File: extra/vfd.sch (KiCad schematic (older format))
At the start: 20 parts

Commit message: more updates, mostly notes and input/output direction changes
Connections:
- net 5v is gone; now on net VCC: P?.2 (P2)
- net GND: now also U?.19 (CE)
- net VCC: now also U?.1 (A->B)
- net vfdD7: now also U?.9 (A7)
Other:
- note added: "NOTE should protect digital ins and outs.. resistors on outs.. diodes on both ins and outs?"
- note added: "NOTE\n\nTo ensure the high-impedance state during power up or power down, OE should be tied to VCC through a pull-up resistor;\nthe minimum value of the resistor is determined by the current-sinking capability of the driver.\n\nboth input and output chips indicate this"

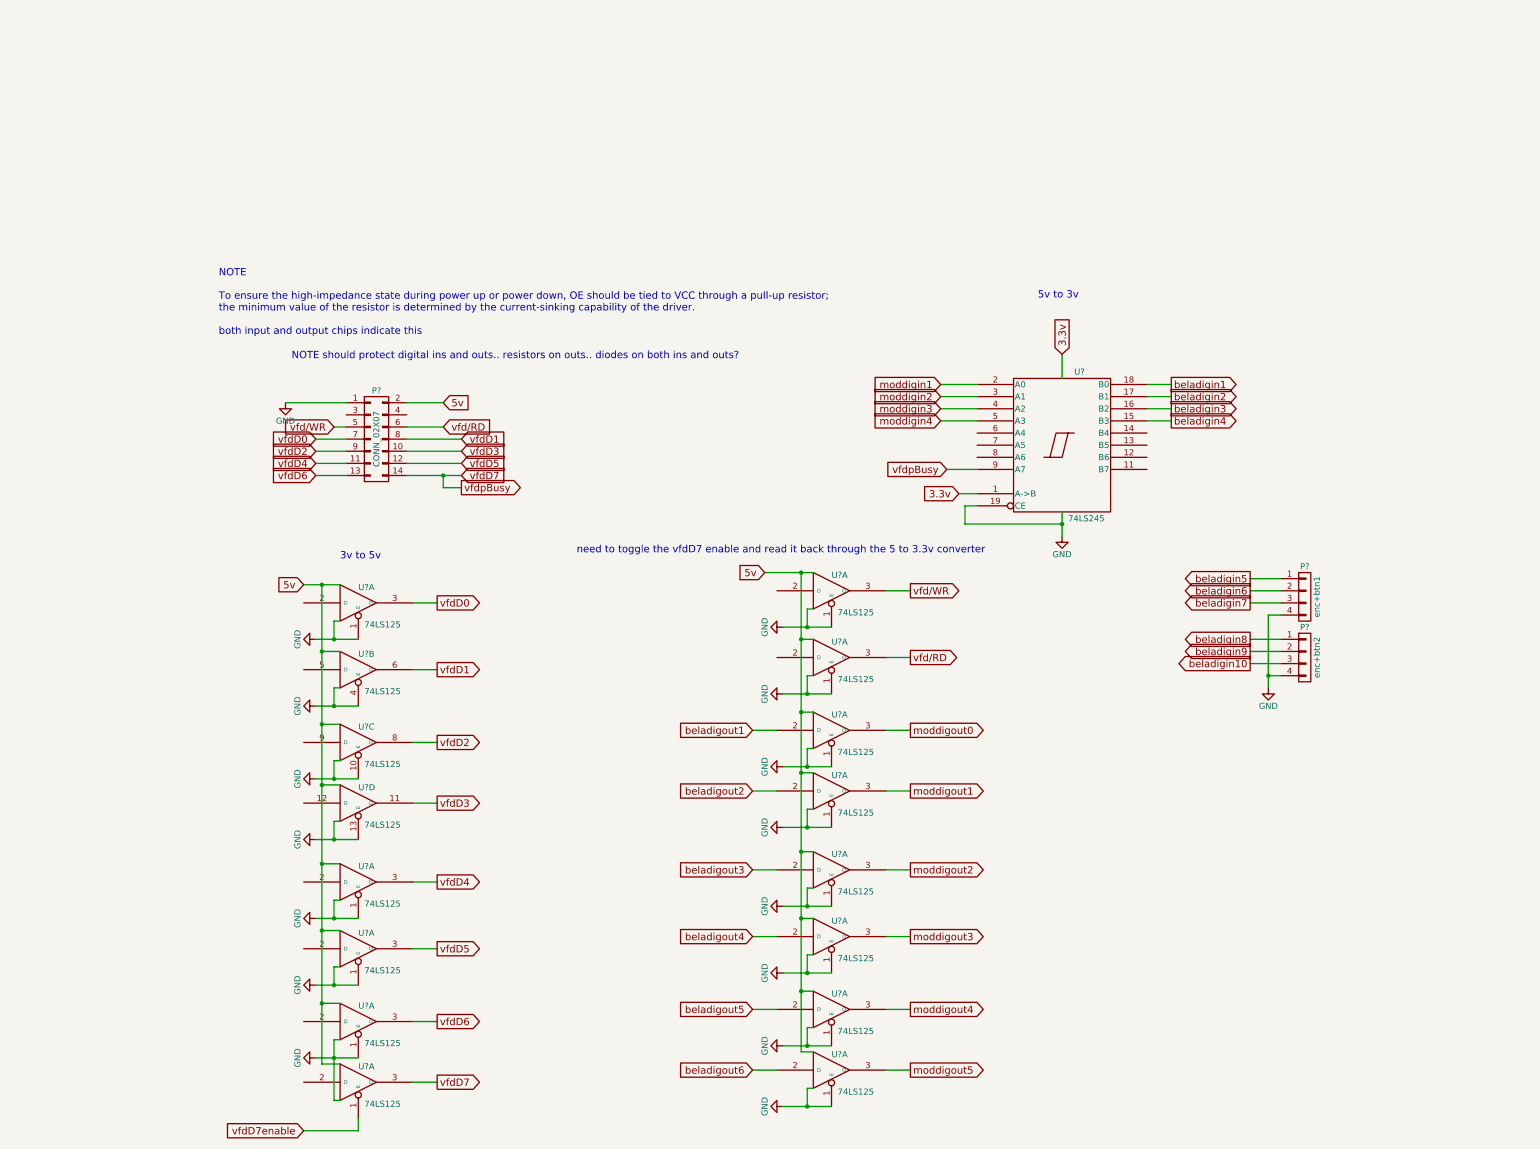
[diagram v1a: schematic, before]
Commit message: much more work on vfd [2 parallel interfaces]
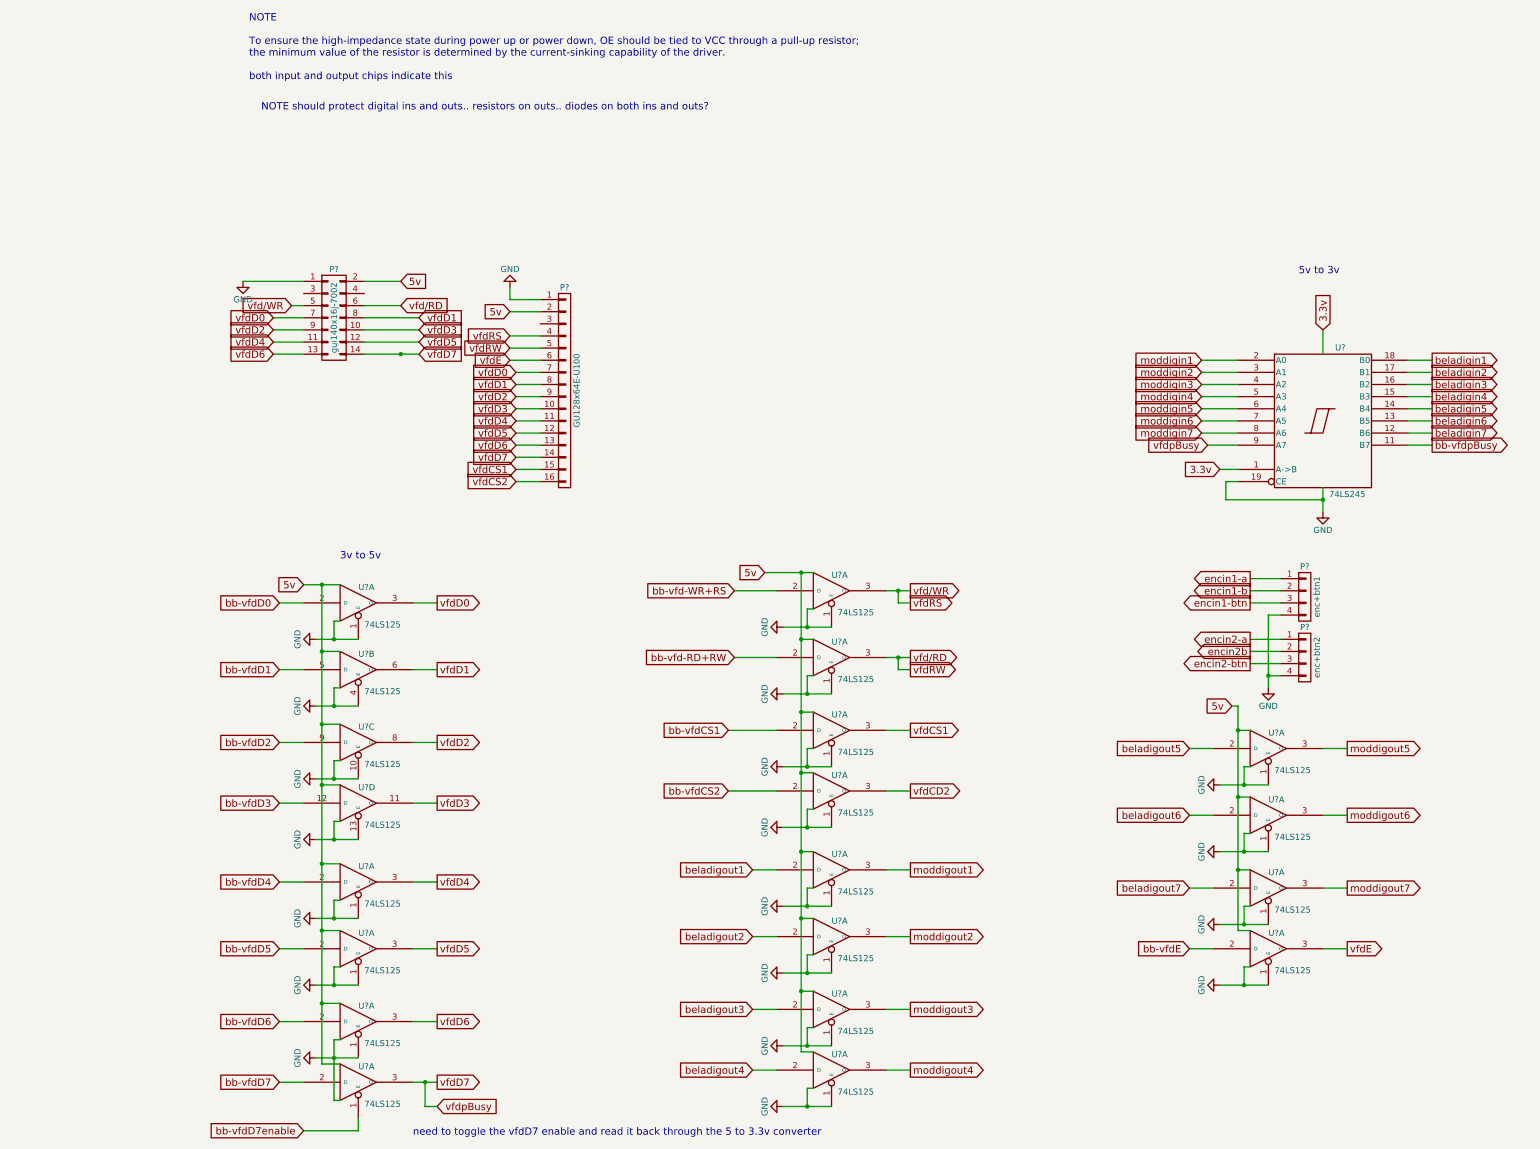
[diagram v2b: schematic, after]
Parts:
- added P?: GU128x64E-U100, symbol CONN_01X16
- added U? (x4): 74LS125, symbol 74LS125
- P?: value CONN_02X07 -> gui140x16j-7002
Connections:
- net GND: now also P?.1 (P1), U?.1 (E), U?.1 (E), U?.1 (E), U?.1 (E), U?.7 (GND), U?.7 (GND), U?.7 (GND), U?.7 (GND)
- net VCC: now also P?.2 (P2), U?.14 (VCC), U?.14 (VCC), U?.14 (VCC), U?.14 (VCC)
- net beladigin5: now also U?.14 (B4); no longer P?.1 (P1)
- net beladigin6: now also U?.13 (B5); no longer P?.2 (P2)
- net beladigin7: now also U?.12 (B6); no longer P?.3 (P3)
- net beladigout1: now also U?.2 (D); no longer U?.2 (D)
- net beladigout2: now also U?.2 (D); no longer U?.2 (D)
- net beladigout3: now also U?.2 (D); no longer U?.2 (D)
- net beladigout4: now also U?.2 (D); no longer U?.2 (D)
- net beladigout5: now also U?.2 (D); no longer U?.2 (D)
- net beladigout6: now also U?.2 (D); no longer U?.2 (D)
- net moddigout1: now also U?.3 (O); no longer U?.3 (O)
- net moddigout2: now also U?.3 (O); no longer U?.3 (O)
- net moddigout3: now also U?.3 (O); no longer U?.3 (O)
- net moddigout4: now also U?.3 (O); no longer U?.3 (O)
- net moddigout5: now also U?.3 (O); no longer U?.3 (O)
- net vfd/RD: now also P?.5 (P5)
- net vfd/WR: now also P?.4 (P4)
- net vfdD0: now also P?.7 (P7)
- net vfdD1: now also P?.8 (P8)
- net vfdD2: now also P?.9 (P9)
- net vfdD3: now also P?.10 (P10)
- net vfdD4: now also P?.11 (P11)
- net vfdD5: now also P?.12 (P12)
- net vfdD6: now also P?.13 (P13)
- net vfdD7: now also P?.14 (P14)
- net bb-vfdD0: now reaches U?.2 (D)
- net bb-vfdD1: now reaches U?.5 (D)
- net bb-vfdD2: now reaches U?.9 (D)
- net bb-vfdD3: now reaches U?.12 (D)
- net bb-vfdD4: now reaches U?.2 (D)
- net bb-vfdD5: now reaches U?.2 (D)
- net bb-vfdD6: now reaches U?.2 (D)
- net bb-vfdD7: now reaches U?.2 (D)
- net bb-vfd-WR+RS: now reaches U?.2 (D)
- net bb-vfd-RD+RW: now reaches U?.2 (D)
- net bb-vfdpBusy: now reaches U?.11 (B7)
- net moddigin5: now reaches U?.6 (A4)
- net moddigin6: now reaches U?.7 (A5)
- net moddigin7: now reaches U?.8 (A6)
- net beladigin10 renamed encin2-btn
- net beladigin8 renamed encin2-a
- net beladigin9 renamed encin2b
- net moddigout0 renamed vfdCS1
- net vfdCS1: now also P?.15 (P15)
- net vfdD7enable renamed bb-vfdD7enable
- new net bb-vfdCS1: U?.2 (D)
- new net bb-vfdCS2: U?.2 (D)
- new net bb-vfdE: U?.2 (D)
- new net beladigout7: U?.2 (D)
- new net encin1-a: P?.1 (P1)
- new net encin1-b: P?.2 (P2)
- new net encin1-btn: P?.3 (P3)
- new net moddigout6: U?.3 (O)
- new net moddigout7: U?.3 (O)
- new net vfdCD2: U?.3 (O)
- new net vfdCS2: P?.16 (P16)
- new net vfdE: P?.6 (P6), U?.3 (O)
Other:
- moved on the sheet: P?, U?

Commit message: a bunch more hooking up
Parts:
- added D? (x14): D, symbol D
- added P?: digital_in, symbol CONN_01X08
- added P?: digital_out, symbol CONN_01X08
- added R? (x14): 20k, symbol R
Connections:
- net GND: now also D?.2 (A), D?.2 (A), D?.2 (A), D?.2 (A), D?.2 (A), D?.2 (A), D?.2 (A), P?.8 (P8), P?.8 (P8)
- net VCC: now also D?.1 (K), D?.1 (K), D?.1 (K), D?.1 (K), D?.1 (K), D?.1 (K), D?.1 (K)
- net moddigin1: now also D?.1 (K), D?.2 (A), R?.1
- net moddigin2: now also D?.1 (K), D?.2 (A), R?.1
- net moddigin3: now also D?.1 (K), D?.2 (A), R?.1
- net moddigin4: now also D?.1 (K), D?.2 (A), R?.1
- net moddigin5: now also D?.1 (K), D?.2 (A), R?.1
- net moddigin6: now also D?.1 (K), D?.2 (A), R?.1
- net moddigin7: now also D?.1 (K), D?.2 (A), R?.1
- net moddigout1: now also R?.1
- net moddigout2: now also R?.1
- net moddigout3: now also R?.1
- net moddigout4: now also R?.1
- net moddigout5: now also R?.1
- net moddigout6: now also R?.1
- net moddigout7: now also R?.1
- new net: P?.1 (P1), R?.2 (x2)
- new net: P?.2 (P2), R?.2 (x2)
- new net: P?.3 (P3), R?.2 (x2)
- new net: P?.4 (P4), R?.2 (x2)
- new net: P?.5 (P5), R?.2 (x2)
- new net: P?.6 (P6), R?.2 (x2)
- new net: P?.7 (P7), R?.2 (x2)
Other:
- note added: "digital input protection, needed if we're using level shifter???"
- note removed: "NOTE should protect digital ins and outs.. resistors on outs.. diodes on both ins and outs?"

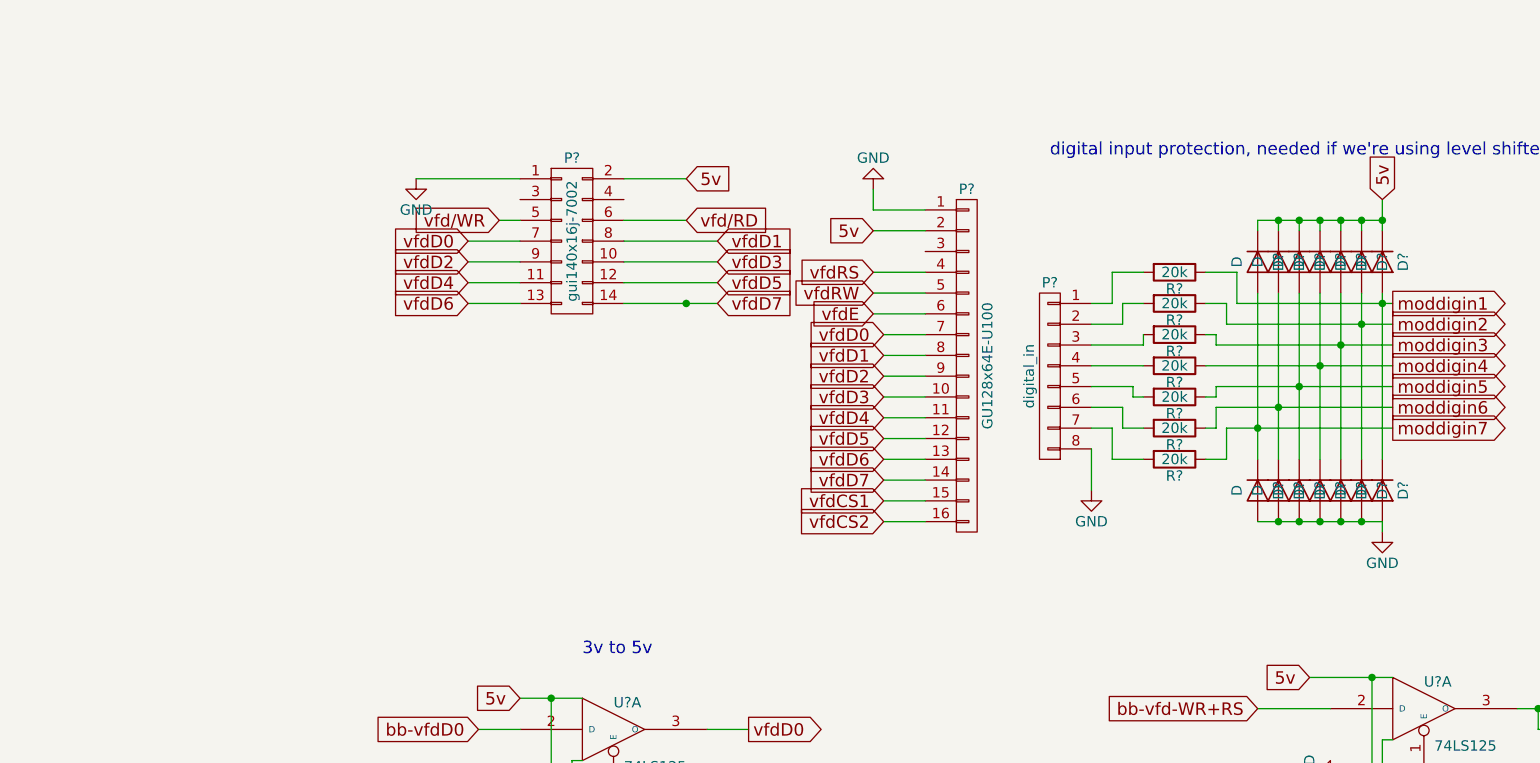
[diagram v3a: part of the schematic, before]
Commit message: added pulldowns for digital inputs
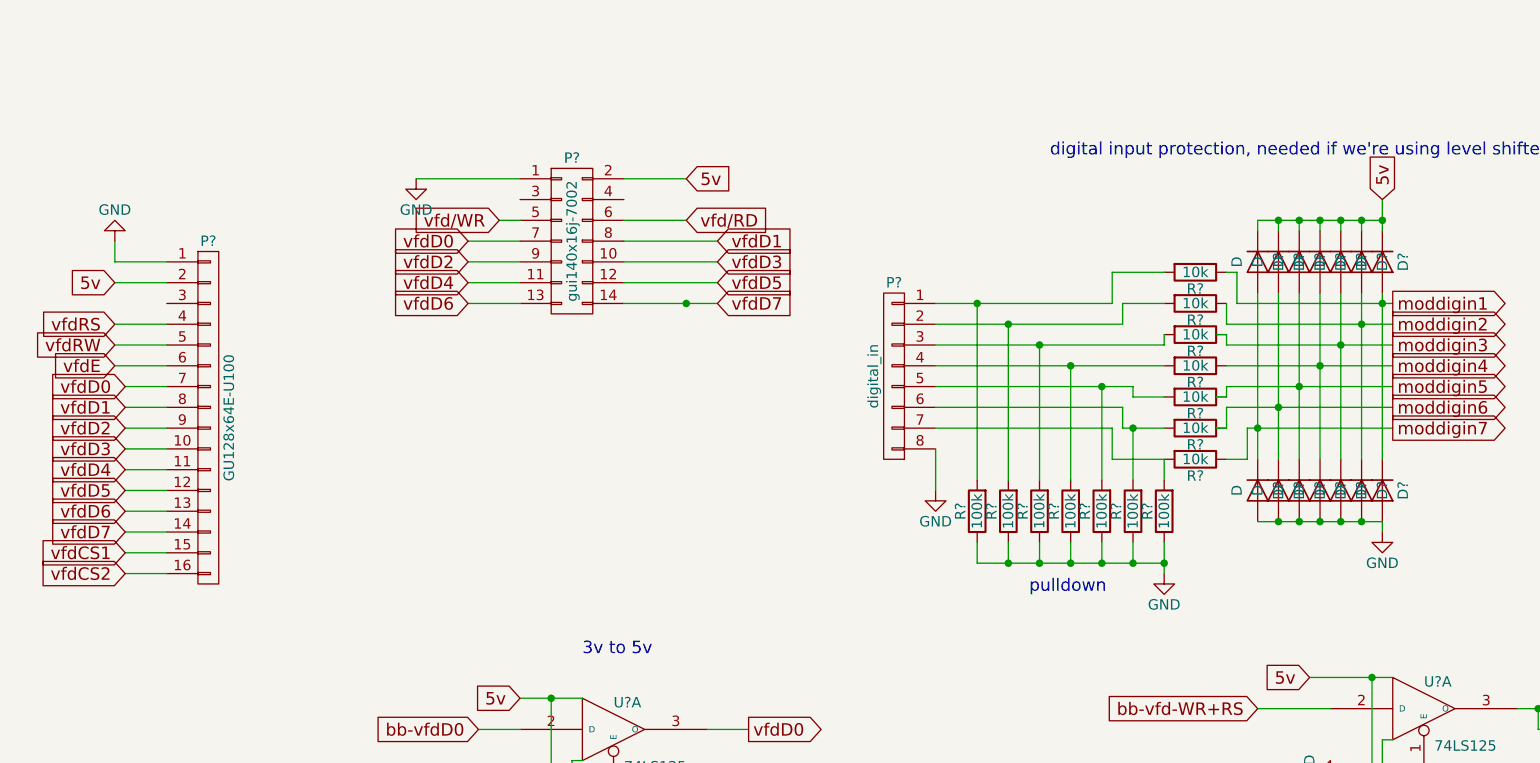
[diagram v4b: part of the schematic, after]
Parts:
- added R? (x7): 100k, symbol R
- R? (x7): value 20k -> 10k
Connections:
- net GND: now also R?.1, R?.1, R?.1, R?.1, R?.1, R?.1, R?.1
- net at P?.1 (P1), R?.2: now also R?.2
- net at P?.2 (P2), R?.2: now also R?.2
- net at P?.3 (P3), R?.2: now also R?.2
- net at P?.4 (P4), R?.2: now also R?.2
- net at P?.5 (P5), R?.2: now also R?.2
- net at P?.6 (P6), R?.2: now also R?.2
- net at P?.7 (P7), R?.2: now also R?.2
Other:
- note added: "pulldown"
- moved on the sheet: P?, R?

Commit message: a lot more layout work
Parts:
- removed D? (x2): D, symbol D
- removed P?: enc+btn1, symbol CONN_01X04
- removed P?: enc+btn2, symbol CONN_01X04
- removed P?: digital_in, symbol CONN_01X08
- removed R?: 10k, symbol R
- removed R?: 100k, symbol R
- added P12: digital_in, symbol CONN_01X07
- added R40: R?, xnorman:Resistor_Horizontal_RM10mm-xnorman, symbol R
- R21, R22, R23, R24, R25, R26, R27, R28, R29, R30, R31, R32, R33, R34, R35, R36, R37, R38, R39: renamed from R?; footprint (none) -> xnorman:Resistor_Horizontal_RM10mm-xnorman
- gave numbers to parts that had none: 21
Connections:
- net GND: now also U4.10 (E), U4.4 (E), U5.10 (E), U5.13 (E), U5.4 (E), U6.10 (E), U6.13 (E), U6.4 (E), U7.10 (E), U7.13 (E), U7.4 (E), P12.7 (P7), R40.1; no longer U4.1 (E), U4.1 (E), U5.1 (E), U5.1 (E), U5.1 (E), U6.1 (E), U6.1 (E), U6.1 (E), U7.1 (E), U7.1 (E), U7.1 (E)
- net bb-vfd-RD+RW: now also U5.5 (D); no longer U5.2 (D)
- net bb-vfdCS1: now also U5.9 (D); no longer U5.2 (D)
- net bb-vfdCS2: now also U5.12 (D); no longer U5.2 (D)
- net bb-vfdD5: now also U4.5 (D); no longer U4.2 (D)
- net bb-vfdD6: now also U4.9 (D); no longer U4.2 (D)
- net bb-vfdD7: now also U4.12 (D); no longer U4.2 (D)
- net bb-vfdD7enable: now also U4.13 (E); no longer U4.1 (E)
- net bb-vfdE: now also U7.12 (D); no longer U7.2 (D)
- net beladigout2: now also U6.5 (D); no longer U6.2 (D)
- net beladigout3: now also U6.9 (D); no longer U6.2 (D)
- net beladigout4: now also U6.12 (D); no longer U6.2 (D)
- net beladigout6: now also U7.5 (D); no longer U7.2 (D)
- net beladigout7: now also U7.9 (D); no longer U7.2 (D)
- net moddigout2: now also U6.6 (O); no longer U6.3 (O)
- net moddigout3: now also U6.8 (O); no longer U6.3 (O)
- net moddigout4: now also U6.11 (O); no longer U6.3 (O)
- net moddigout6: now also U7.6 (O); no longer U7.3 (O)
- net moddigout7: now also U7.8 (O); no longer U7.3 (O)
- net vfd/RD: now also U5.6 (O); no longer U5.3 (O)
- net vfdCS1: now also U5.8 (O); no longer U5.3 (O)
- net vfdCS2: now also U5.11 (O)
- net vfdD5: now also U4.6 (O); no longer U4.3 (O)
- net vfdD6: now also U4.8 (O); no longer U4.3 (O)
- net vfdD7: now also U4.11 (O); no longer U4.3 (O)
- net vfdE: now also U7.11 (O); no longer U7.3 (O)
- net at R21.2, R27.2: now also P12.1 (P1)
- net at R22.2, R28.2: now also P12.2 (P2)
- net at R23.2, R29.2: now also P12.3 (P3)
- net at R24.2, R30.2: now also P12.4 (P4)
- net at R25.2, R31.2: now also P12.5 (P5)
- net at R26.2, R32.2: now also P12.6 (P6)
- net beladigin7: no longer names the net of U8.12 (B6)
- net moddigin7: no longer names the net of U8.8 (A6)
- net moddigin7: now also R40.2
- removed net vfdCD2: U5.3 (O)
- no-connect marks 0 -> 4
